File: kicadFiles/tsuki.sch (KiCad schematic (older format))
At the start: 203 parts, among them J1 TYPE-C-31-M12_13, J2 Conn_01x14, J3 Conn_ARM_JTAG_SWD_10, SW1 ESC, SW10 9, SW11 0, SW12 -_, SW13 +=, SW14 2U BKSP, SW15 TAB_150, SW16 Q, SW17 W, SW18 E, SW19 R, SW2 1, SW20 T, SW21 Y, SW22 U, SW23 I, SW24 O, SW25 P, SW26 [{, SW27 ]}, SW28 \\|_150, SW29 CAPS_175, SW3 2, SW30 A, SW31 S, SW32 D, SW33 F, SW34 G, SW35 H, SW36 J, SW37 K, SW38 L, SW39 :;, SW4 3, SW40 \"', SW41 ENTER_225, SW42 LSHIFT_225, SW43 Z, SW44 X, SW45 C, SW46 V, SW47 B, SW48 N, SW49 M, SW5 4, SW50 <,, SW51 >., SW52 ?/, SW53 RSHIFT_275, SW54 LCTRL_150, SW55 LGUI_100, SW56 LALT_150, SW57 SPACE_600, SW58 RALT_150, SW59 RGUI_150, SW6 5, SW60 RCTRL_150, SW61 FN_100, SW62 RSHIFT_175, SW63 STEPPED_CAPS_125, SW64 1U LBKSP, SW65 1U RBKSP, SW66 ISO_100, SW67 ISO_ENTER, SW68 LCTRL_125, SW69 LGUI_125, SW7 6, SW70 LGUI_100, SW71 LALT_125, SW72 LALT_150, SW73 SPACE_225, SW74 SPACE_225, SW75 SPACE_625, SW76 SPACE_125, SW77 SPACE_700, SW78 SPACE_275, SW79 SPACE_275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

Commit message: Removed split space options
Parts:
- removed D63, D64: 1N4148, acheron_Components:D_SOD-123, symbol Device:D
- removed SW73, SW74: SPACE_225, acheron_MX_SolderMask:MX225R, symbol acheronSymbols:MXSwitch
- removed SW76: SPACE_125, acheron_MX_SolderMask:MX125, symbol acheronSymbols:MXSwitch
- removed SW78, SW79: SPACE_275, acheron_MX_SolderMask:MX275R, symbol acheronSymbols:MXSwitch
- removed SW82: RALT_150, acheron_MX_SolderMask:MX150, symbol acheronSymbols:MXSwitch
- removed SW85: RGUI_125, acheron_MX_SolderMask:MX125, symbol acheronSymbols:MXSwitch
- removed SW87: RCTRL_125, acheron_MX_SolderMask:MX125, symbol acheronSymbols:MXSwitch
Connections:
- net labels removed: L4
- wire segments 446 -> 424
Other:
- note removed: "225-125-275 Bottom"
- note removed: "225-275 Bottom"

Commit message: Remove layouts, update li, add label, maintenance
- The split backspace layouts were removed. This decision was made because I reckoned a very small amount of people would use them, and the PCB is already very compromised material-wise as it is.

- The Acheron Library was updated, following the updates in other projects

- A label was added signalling the pre-Revision Alpha

- The footprints for the holes were all changed for the no-backside version, to avoid any unintended short-circuits

- Indicative documentation and arrows were added for the bottom row layouts to facilitate building the PCB
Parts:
- added L4: TsukiLabel, tsukiGraphics:tsukiLabel_30x12mm, symbol Mechanical:MountingHole
- H10, H2, H3, H5, H7, H9: footprint acheron_MountingHoles:MoutingHole_Oval_7mm_5.0x2.5mm -> acheron_MountingHoles:MoutingHole_Oval_BackOnly_7mm_5.0x2.5mm
- L2: footprint oshLogo:osh-logo -> acheron_Graphics:osh-logo
- RGUI_125, SW1, SW10, SW11, SW12, SW13, SW14, SW15, SW16, SW17, SW18, SW19, SW2, SW20, SW21, SW22, SW23, SW24, SW25, SW26, SW27, SW28, SW29, SW3, SW30, SW31, SW32, SW33, SW34, SW35, SW36, SW37, SW38, SW39, SW4, SW40, SW41, SW42, SW43, SW44, SW45, SW46, SW47, SW48, SW49, SW5, SW50, SW51, SW52, SW53, SW54, SW55, SW56, SW57, SW58, SW59, SW6, SW60, SW61, SW62, SW63, SW64, SW65, SW66, SW67, SW68, SW69, SW7, SW70, SW71, SW72, SW75, SW77, SW8, SW80, SW81, SW83, SW84, SW86, SW88, SW89, SW9: symbol acheronSymbols:MXSwitch -> tsuki-rescue:MXSwitch-acheronSymbols
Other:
- note added: "6.25U Bottom (D for default ANSI)"
- note added: "6U Bottom (H for HHKB)"
- note added: "7U Bottom (T for Tsangan bottom)"
- note removed: "6.25U Bottom"
- note removed: "6U Bottom"
- note removed: "7U Bottom"

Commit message: Added Schottky diodes and TVS
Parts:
- removed CUSB1: 100n, Capacitor_SMD:C_0805_2012Metric_Pad1.15x1.40mm_HandSolder, symbol Device:C_Small
- CSI1, CSO1: value 100n -> 1u
- DF1: value RB060M-60TR -> SMF9.0CA; symbol Device:D_Schottky -> Device:D_TVS
- DS1: value 1N4148 -> RB060M-60TR; symbol Device:D -> Device:D_Schottky
- DSH1: value 1N4007 -> RB060M-60TR; symbol Device:D -> Device:D_Schottky
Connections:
- wire segments 424 -> 421
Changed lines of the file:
@@
 P 8475 20600
 F 0 "CSI1" V 8575 20600 39  0000 C CNN
-F 1 "100n" V 8375 20600 31  0000 C CNN
+F 1 "1u" V 8375 20600 31  0000 C CNN
 F 2 "Capacitor_SMD:C_0805_2012Metric_Pad1.15x1.40mm_HandSolder" H 8475 20600 50  0001 C CNN
 F 3 "~" H 8475 20600 50  0001 C CNN
@@
 	-1   0    0    1
 $EndComp
-$Comp
-L Device:C_Small CSO1
-U 1 1 5C44DAFA
-P 9175 20625
-F 0 "CSO1" V 9275 20625 39  0000 C CNN
-F 1 "100n" V 9050 20625 39  0000 C CNN
-F 2 "Capacitor_SMD:C_0805_2012Metric_Pad1.15x1.40mm_HandSolder" H 9175 20625 50  0001 C CNN
-F 3 "~" H 9175 20625 50  0001 C CNN
-	1    9175 20625
-	-1   0    0    1
-$EndComp
 Wire Wire Line
 	9175 20250 9175 20525
@@
 	7275 19350 10250 19350
 $Comp
-L Device:D DS1
+L Device:D_Schottky DS1
 U 1 1 5C44EA7A
 P 8825 19775
 F 0 "DS1" V 8794 19854 31  0000 L CNN
-F 1 "1N4148" V 8856 19854 31  0000 L CNN
+F 1 "RB060M-60TR" V 8856 19854 31  0000 L CNN
 F 2 "acheron_Components:D_SOD-123" H 8825 19775 50  0001 C CNN
 F 3 "~" H 8825 19775 50  0001 C CNN
@@
 Wire Wire Line
 	5725 15175 5775 15175
-$Comp
-L Device:C_Small CUSB1
-U 1 1 5E01896F
-P 5375 14725
-F 0 "CUSB1" V 5275 14725 31  0000 C CNN
-F 1 "100n" V 5475 14725 31  0000 C CNN
-F 2 "Capacitor_SMD:C_0805_2012Metric_Pad1.15x1.40mm_HandSolder" H 5375 14725 50  0001 C CNN
-F 3 "~" H 5375 14725 50  0001 C CNN
-	1    5375 14725
-	0    1    1    0
-$EndComp
-Wire Wire Line
-	5225 14775 5225 14725
-Wire Wire Line
-	5275 14725 5225 14725
-Connection ~ 5225 14725
-Wire Wire Line
-	5475 14725 5525 14725
-$Comp
-L power:GND #PWR0112
-U 1 1 5E173141
-P 5525 14725
-F 0 "#PWR0112" H 5525 14475 50  0001 C CNN
-F 1 "GND" H 5525 14600 31  0000 C CNN
-F 2 "" H 5525 14725 50  0001 C CNN
-F 3 "" H 5525 14725 50  0001 C CNN
-	1    5525 14725
-	0    -1   -1   0
-$EndComp
 Text GLabel 5225 14650 1    50   Input ~ 0
 VBUS
-Wire Wire Line
-	5225 14650 5225 14725
 $Comp
 L power:GND #PWR0113
@@
 $EndComp
 $Comp
-L Device:D_Schottky DF1
+L Device:D_TVS DF1
 U 1 1 5ECEA097
 P 8100 20425
 F 0 "DF1" H 8050 20250 50  0000 L CNN
-F 1 "RB060M-60TR" H 7975 20325 30  0000 L CNN
+F 1 "SMF9.0CA" H 7975 20325 30  0000 L CNN
 F 2 "acheron_Components:D_SOD-123" H 8100 20425 50  0001 C CNN
 F 3 "~" H 8100 20425 50  0001 C CNN
@@
 $EndComp
 $Comp
-L Device:D DSH1
+L Device:D_Schottky DSH1
 U 1 1 5D48318C
 P 11575 17250
 F 0 "DSH1" V 11544 17329 31  0000 L CNN
-F 1 "1N4007" V 11606 17329 31  0000 L CNN
+F 1 "RB060M-60TR" V 11606 17329 31  0000 L CNN
 F 2 "acheron_Components:D_SOD-123" H 11575 17250 50  0001 C CNN
 F 3 "~" H 11575 17250 50  0001 C CNN
@@
 	1    0    0    -1
 $EndComp
+$Comp
+L Device:C_Small CSO1
+U 1 1 5C44DAFA
+P 9175 20625
+F 0 "CSO1" V 9275 20625 39  0000 C CNN
+F 1 "1u" V 9050 20625 39  0000 C CNN
+F 2 "Capacitor_SMD:C_0805_2012Metric_Pad1.15x1.40mm_HandSolder" H 9175 20625 50  0001 C CNN
+F 3 "~" H 9175 20625 50  0001 C CNN
+	1    9175 20625
+	-1   0    0    1
+$EndComp
+Wire Wire Line
+	5225 14650 5225 14775
 $EndSCHEMATC

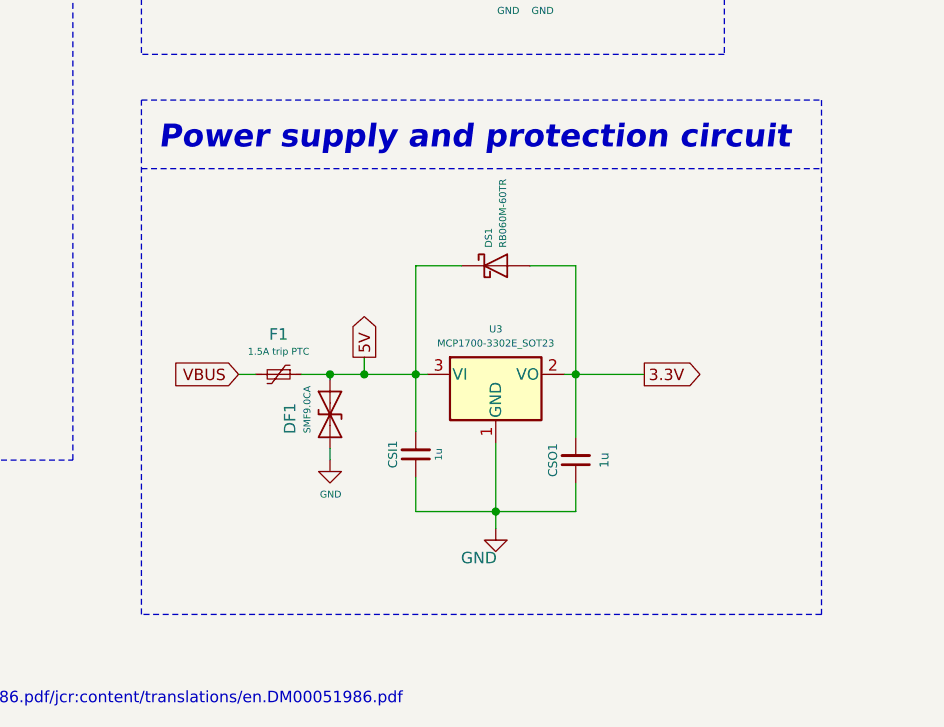
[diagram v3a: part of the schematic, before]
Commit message: Added discharge resistors RSI and RSO
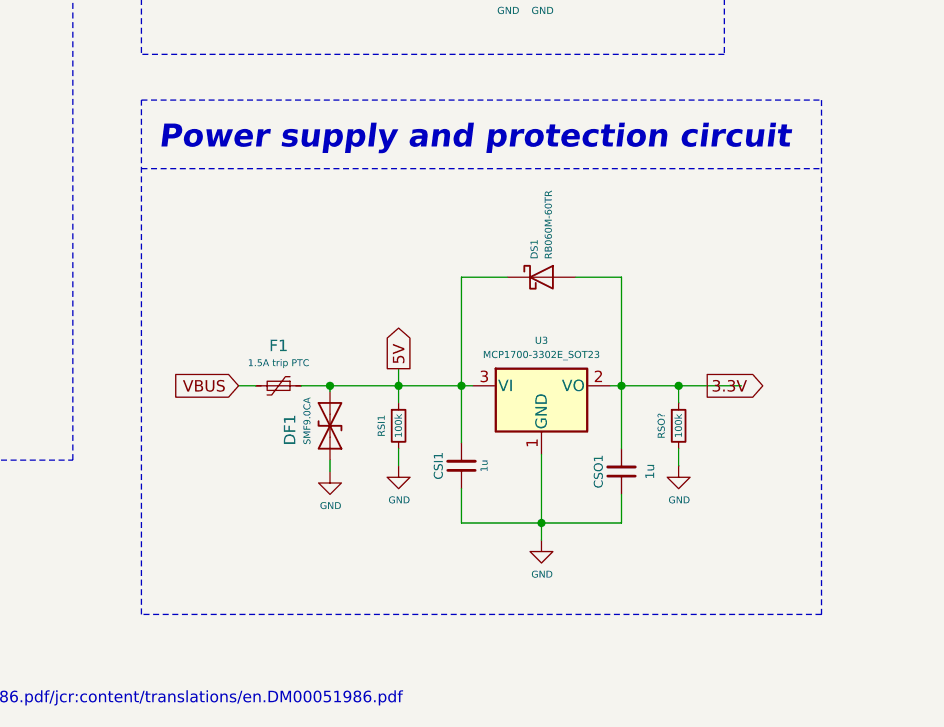
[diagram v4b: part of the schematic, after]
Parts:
- added RSI1, RSO?: 100k, acheron_Components:R_SMD_1206, symbol Device:R_Small
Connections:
- wire segments 421 -> 426
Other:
- moved on the sheet: CSI1, CSO1, DF1, DS1, F1, U3
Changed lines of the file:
@@
 L Device:C_Small CSI1
 U 1 1 5C44CEDC
-P 8475 20600
-F 0 "CSI1" V 8575 20600 39  0000 C CNN
-F 1 "1u" V 8375 20600 31  0000 C CNN
-F 2 "Capacitor_SMD:C_0805_2012Metric_Pad1.15x1.40mm_HandSolder" H 8475 20600 50  0001 C CNN
-F 3 "~" H 8475 20600 50  0001 C CNN
-	1    8475 20600
+P 8675 20650
+F 0 "CSI1" V 8775 20650 39  0000 C CNN
+F 1 "1u" V 8575 20650 31  0000 C CNN
+F 2 "Capacitor_SMD:C_0805_2012Metric_Pad1.15x1.40mm_HandSolder" H 8675 20650 50  0001 C CNN
+F 3 "~" H 8675 20650 50  0001 C CNN
+	1    8675 20650
 	-1   0    0    1
 $EndComp
 Wire Wire Line
-	9175 20250 9175 20525
+	9375 20300 9375 20575
 Wire Wire Line
-	8525 20250 8475 20250
+	8725 20300 8675 20300
 Wire Wire Line
-	8475 20250 8475 20500
-Connection ~ 8475 20250
+	8675 20300 8675 20550
+Connection ~ 8675 20300
 Wire Wire Line
-	8475 20250 8475 19775
-Wire Wire Line
-	8250 20250 8475 20250
-Text GLabel 9475 20250 2    50   Output ~ 0
+	8675 20300 8675 19825
+Text GLabel 9750 20300 2    50   Output ~ 0
 3.3V
 Text GLabel 20275 16700 2    50   BiDi ~ 0
@@
 L Regulator_Linear:MCP1700-3302E_SOT23 U3
 U 1 1 5D83639E
-P 8825 20250
-F 0 "U3" H 8825 20448 31  0000 C CNN
-F 1 "MCP1700-3302E_SOT23" H 8825 20386 31  0000 C CNN
-F 2 "Package_TO_SOT_SMD:SOT-23" H 8825 20475 50  0001 C CNN
-F 3 "http://ww1.microchip.com/downloads/en/DeviceDoc/20001826C.pdf" H 8825 20250 50  0001 C CNN
-	1    8825 20250
+P 9025 20300
+F 0 "U3" H 9025 20498 31  0000 C CNN
+F 1 "MCP1700-3302E_SOT23" H 9025 20436 31  0000 C CNN
+F 2 "Package_TO_SOT_SMD:SOT-23" H 9025 20525 50  0001 C CNN
+F 3 "http://ww1.microchip.com/downloads/en/DeviceDoc/20001826C.pdf" H 9025 20300 50  0001 C CNN
+	1    9025 20300
 	1    0    0    -1
 $EndComp
 Wire Wire Line
-	8475 20700 8475 20850
+	8675 20750 8675 20900
 Wire Wire Line
-	9175 20850 9175 20725
+	9375 20900 9375 20775
 Wire Wire Line
-	8825 20550 8825 20850
-Connection ~ 8825 20850
+	9025 20600 9025 20900
+Connection ~ 9025 20900
 Wire Wire Line
-	9125 20250 9175 20250
-$Comp
-L power:GND #PWR018
-U 1 1 5D9C16B4
-P 8825 20925
-F 0 "#PWR018" H 8825 20675 50  0001 C CNN
-F 1 "GND" H 8830 20797 50  0000 R CNN
-F 2 "" H 8825 20925 50  0001 C CNN
-F 3 "" H 8825 20925 50  0001 C CNN
-	1    8825 20925
-	1    0    0    -1
-$EndComp
+	9325 20300 9375 20300
 Wire Wire Line
-	8825 20925 8825 20850
+	9025 20975 9025 20900
 $Comp
 L Switch:SW_Push SWRST1
@@
 Text Notes 7350 19275 0    100  Italic 20
 Power supply and protection circuit
-Text GLabel 8250 20175 1    50   Output ~ 0
+Text GLabel 8400 20225 1    50   Output ~ 0
 5V
 Wire Wire Line
-	8250 20175 8250 20250
+	8400 20225 8400 20300
 Wire Wire Line
-	8975 19775 9175 19775
+	9175 19825 9375 19825
 Wire Wire Line
-	8475 19775 8675 19775
+	8675 19825 8875 19825
 Wire Wire Line
-	9175 20250 9175 19775
-Connection ~ 9175 20250
+	9375 20300 9375 19825
+Connection ~ 9375 20300
 Wire Wire Line
-	8825 20850 9175 20850
+	9025 20900 9375 20900
 Wire Wire Line
-	9175 20250 9475 20250
-Wire Wire Line
-	8825 20850 8475 20850
+	9025 20900 8675 20900
 Text GLabel 7900 18150 0    50   Input ~ 0
 3.3V
@@
 L Device:D_Schottky DS1
 U 1 1 5C44EA7A
-P 8825 19775
-F 0 "DS1" V 8794 19854 31  0000 L CNN
-F 1 "RB060M-60TR" V 8856 19854 31  0000 L CNN
-F 2 "acheron_Components:D_SOD-123" H 8825 19775 50  0001 C CNN
-F 3 "~" H 8825 19775 50  0001 C CNN
-	1    8825 19775
+P 9025 19825
+F 0 "DS1" V 8994 19904 31  0000 L CNN
+F 1 "RB060M-60TR" V 9056 19904 31  0000 L CNN
+F 2 "acheron_Components:D_SOD-123" H 9025 19825 50  0001 C CNN
+F 3 "~" H 9025 19825 50  0001 C CNN
+	1    9025 19825
 	1    0    0    -1
 $EndComp
@@
 L Device:Polyfuse_Small F1
 U 1 1 5ECE83A7
-P 7875 20250
-F 0 "F1" V 7700 20250 50  0000 C CNN
-F 1 "1.5A trip PTC" V 7775 20250 30  0000 C CNN
-F 2 "acheron_Components:Fuse_1812_4532" H 7925 20050 50  0001 L CNN
-F 3 "~" H 7875 20250 50  0001 C CNN
-	1    7875 20250
+P 7875 20300
+F 0 "F1" V 7700 20300 50  0000 C CNN
+F 1 "1.5A trip PTC" V 7775 20300 30  0000 C CNN
+F 2 "acheron_Components:Fuse_1812_4532" H 7925 20100 50  0001 L CNN
+F 3 "~" H 7875 20300 50  0001 C CNN
+	1    7875 20300
 	0    1    1    0
 $EndComp
@@
 L Device:D_TVS DF1
 U 1 1 5ECEA097
-P 8100 20425
-F 0 "DF1" H 8050 20250 50  0000 L CNN
-F 1 "SMF9.0CA" H 7975 20325 30  0000 L CNN
-F 2 "acheron_Components:D_SOD-123" H 8100 20425 50  0001 C CNN
-F 3 "~" H 8100 20425 50  0001 C CNN
-	1    8100 20425
+P 8100 20475
+F 0 "DF1" H 8050 20300 50  0000 L CNN
+F 1 "SMF9.0CA" H 7975 20375 30  0000 L CNN
+F 2 "acheron_Components:D_SOD-123" H 8100 20475 50  0001 C CNN
+F 3 "~" H 8100 20475 50  0001 C CNN
+	1    8100 20475
 	0    1    1    0
 $EndComp
 Wire Wire Line
-	7975 20250 8100 20250
-Connection ~ 8250 20250
-Wire Wire Line
-	8100 20250 8100 20275
+	7975 20300 8100 20300
 Wire Wire Line
-	8100 20575 8100 20625
-Connection ~ 8100 20250
+	8100 20300 8100 20325
 Wire Wire Line
-	8100 20250 8250 20250
+	8100 20625 8100 20675
+Connection ~ 8100 20300
 Wire Wire Line
-	7700 20250 7775 20250
-Text GLabel 7700 20250 0    50   Input ~ 0
+	7700 20300 7775 20300
+Text GLabel 7700 20300 0    50   Input ~ 0
 VBUS
 $Comp
 L power:GND #PWR0110
 U 1 1 5ED7F608
-P 8100 20625
-F 0 "#PWR0110" H 8100 20375 50  0001 C CNN
-F 1 "GND" H 8150 20475 30  0000 R CNN
-F 2 "" H 8100 20625 50  0001 C CNN
-F 3 "" H 8100 20625 50  0001 C CNN
-	1    8100 20625
+P 8100 20675
+F 0 "#PWR0110" H 8100 20425 50  0001 C CNN
+F 1 "GND" H 8150 20525 30  0000 R CNN
+F 2 "" H 8100 20675 50  0001 C CNN
+F 3 "" H 8100 20675 50  0001 C CNN
+	1    8100 20675
 	1    0    0    -1
 $EndComp
@@
 L Device:C_Small CSO1
 U 1 1 5C44DAFA
-P 9175 20625
-F 0 "CSO1" V 9275 20625 39  0000 C CNN
-F 1 "1u" V 9050 20625 39  0000 C CNN
-F 2 "Capacitor_SMD:C_0805_2012Metric_Pad1.15x1.40mm_HandSolder" H 9175 20625 50  0001 C CNN
-F 3 "~" H 9175 20625 50  0001 C CNN
-	1    9175 20625
+P 9375 20675
+F 0 "CSO1" V 9475 20675 39  0000 C CNN
+F 1 "1u" V 9250 20675 39  0000 C CNN
+F 2 "Capacitor_SMD:C_0805_2012Metric_Pad1.15x1.40mm_HandSolder" H 9375 20675 50  0001 C CNN
+F 3 "~" H 9375 20675 50  0001 C CNN
+	1    9375 20675
 	-1   0    0    1
 $EndComp
 Wire Wire Line
 	5225 14650 5225 14775
+$Comp
+L Device:R_Small RSI1
+U 1 1 5DFE1813
+P 8400 20475
+F 0 "RSI1" V 8325 20475 31  0000 C CNN
+F 1 "100k" V 8400 20475 31  0000 C CNN
+F 2 "acheron_Components:R_SMD_1206" H 8400 20475 50  0001 C CNN
+F 3 "~" H 8400 20475 50  0001 C CNN
+	1    8400 20475
+	1    0    0    -1
+$EndComp
+$Comp
+L power:GND #PWR?
+U 1 1 5E04A109
+P 8400 20650
+F 0 "#PWR?" H 8400 20400 50  0001 C CNN
+F 1 "GND" H 8450 20500 30  0000 R CNN
+F 2 "" H 8400 20650 50  0001 C CNN
+F 3 "" H 8400 20650 50  0001 C CNN
+	1    8400 20650
+	1    0    0    -1
+$EndComp
+Wire Wire Line
+	8400 20650 8400 20575
+Wire Wire Line
+	8400 20375 8400 20300
+Connection ~ 8400 20300
+Wire Wire Line
+	8400 20300 8675 20300
+$Comp
+L Device:R_Small RSO?
+U 1 1 5E0E3A96
+P 9625 20475
+F 0 "RSO?" V 9550 20475 31  0000 C CNN
+F 1 "100k" V 9625 20475 31  0000 C CNN
+F 2 "acheron_Components:R_SMD_1206" H 9625 20475 50  0001 C CNN
+F 3 "~" H 9625 20475 50  0001 C CNN
+	1    9625 20475
+	1    0    0    -1
+$EndComp
+$Comp
+L power:GND #PWR?
+U 1 1 5E0E3A9D
+P 9625 20650
+F 0 "#PWR?" H 9625 20400 50  0001 C CNN
+F 1 "GND" H 9675 20500 30  0000 R CNN
+F 2 "" H 9625 20650 50  0001 C CNN
+F 3 "" H 9625 20650 50  0001 C CNN
+	1    9625 20650
+	1    0    0    -1
+$EndComp
+Wire Wire Line
+	9625 20650 9625 20575
+Wire Wire Line
+	9625 20375 9625 20300
+Connection ~ 9625 20300
+Wire Wire Line
+	9625 20300 9900 20300
+Wire Wire Line
+	9375 20300 9625 20300
+$Comp
+L power:GND #PWR?
+U 1 1 5E1B9CA9
+P 9025 20975
+F 0 "#PWR?" H 9025 20725 50  0001 C CNN
+F 1 "GND" H 9075 20825 30  0000 R CNN
+F 2 "" H 9025 20975 50  0001 C CNN
+F 3 "" H 9025 20975 50  0001 C CNN
+	1    9025 20975
+	1    0    0    -1
+$EndComp
+Wire Wire Line
+	8100 20300 8400 20300
 $EndSCHEMATC

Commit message: Added RGB to schematic
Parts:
- added CRGB1, CRGB10, CRGB2, CRGB3, CRGB4, CRGB5, CRGB6, CRGB7, CRGB8, CRGB9: 100n, Capacitor_SMD:C_0805_2012Metric, symbol Device:C_Small
- added Q1: BSS138, Package_TO_SOT_SMD:SOT-23, symbol Transistor_FET:BSS138
- added RGB1, RGB10, RGB2, RGB3, RGB4, RGB5, RGB6, RGB7, RGB8, RGB9: WS2812B, LED_SMD:LED_WS2812B_PLCC4_5.0x5.0mm_P3.2mm, symbol LED:WS2812B
- added RRGB1, RRGB10, RRGB2, RRGB3, RRGB4, RRGB5, RRGB6, RRGB7, RRGB8, RRGB9: 5.1R, acheron_Components:R_SMD_1026, symbol Device:R_Small
- added RS1, RS2: 10k, acheron_Components:R_SMD_1026, symbol Device:R_Small
- gave numbers to parts that had none: 1
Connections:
- net labels added: RGB_3V3, RGB_5V
- wire segments 426 -> 507

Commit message: Added LED control to schematic
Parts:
- removed SW57: SPACE_600, acheron_MX_SolderMask:MX600R, symbol tsuki-rescue:MXSwitch-acheronSymbols
- added LED1: LED, acheron_Components:LED_THT_2.54mm, symbol acheronSymbols:LED
- added Q?: AO4407A, acheron_Components:SOIC-8, symbol tsuki-rescue:AO4407A-acheronSymbols
- added QRST?: DTC123J, Package_TO_SOT_SMD:SOT-23, symbol Transistor_BJT:DTC123J
- added RL1: 420R, acheron_Components:R_SMD_1206, symbol Device:R_Small
- added RLED1, RLED?: 10k, acheron_Components:R_SMD_1206, symbol Device:R_Small
- added RLED?: 100R, acheron_Components:R_SMD_1206, symbol Device:R_Small
- J1: symbol acheronSymbols:TYPE-C-31-M12_13 -> tsuki-rescue:TYPE-C-31-M12_13-acheronSymbols
- RCC1, RCC2, RRGB1, RRGB10, RRGB2, RRGB3, RRGB4, RRGB5, RRGB6, RRGB7, RRGB8, RRGB9, RRST1, RS1, RS2, RSH1, RSH2: footprint acheron_Components:R_SMD_1026 -> acheron_Components:R_SMD_1206
- RGB1, RGB10, RGB2, RGB3, RGB4, RGB5, RGB6, RGB7, RGB8, RGB9: footprint LED_SMD:LED_WS2812B_PLCC4_5.0x5.0mm_P3.2mm -> acheron_Components:LED_WS2812B_5.0x5.0mm_P3.2mm
- U1: symbol acheronSymbols:STM32F072-LQFP48 -> tsuki-rescue:STM32F072-LQFP48-acheronSymbols
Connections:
- net labels added: LED_PWM
- wire segments 507 -> 520
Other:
- note added: "Observation: the 6U spacebar footprint\nis already covered by the 6.25+7U\nspacebar footprints"

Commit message: Added bottom row documentation
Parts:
- added L5, L6, L7, L8, L9: Warning, acheron_Graphics:warning_sign_3.6x3.2mm, symbol Mechanical:MountingHole
- added LED10, LED11, LED12, LED13, LED14, LED15, LED16, LED17, LED18, LED19, LED2, LED20, LED21, LED22, LED23, LED24, LED25, LED26, LED27, LED28, LED29, LED3, LED30, LED31, LED32, LED4, LED5, LED6, LED7, LED8, LED9: LED, acheron_Components:LED_THT_2.54mm, symbol tsuki-rescue:LED-acheronSymbols
- added RL10, RL11, RL12, RL13, RL14, RL16, RL17, RL18, RL19, RL2, RL20, RL21, RL22, RL23, RL24, RL25, RL26, RL27, RL28, RL29, RL3, RL30, RL31, RL32, RL4, RL5, RL6, RL7, RL8, RL9: 420R, acheron_Components:R_SMD_1206, symbol Device:R_Small
- LED1: symbol acheronSymbols:LED -> tsuki-rescue:LED-acheronSymbols
- SW67: footprint acheron_MX_SolderMask:MX_ISOEnter_Vertical -> acheron_MX_SolderMask:MX_ISOEnter_Vertical_LED
- gave numbers to parts that had none: 4
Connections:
- net Col1: now also SW63.2 (Row); no longer SW63.1 (Col)
- net Col2: now also SW55.2 (Row); no longer SW55.1 (Col)
- net GND: now also LED10.K, LED11.K, LED12.K, LED13.K, LED14.K, LED15.K, LED16.K, LED17.K, LED18.K, LED19.K, LED2.K, LED20.K, LED21.K, LED22.K, LED23.K, LED24.K, LED25.K, LED26.K, LED27.K, LED28.K, LED29.K, LED3.K, LED30.K, LED31.K, LED32.K, LED4.K, LED5.K, LED6.K, LED7.K, LED8.K, LED9.K
- net L2: now also SW55.1 (Col); no longer SW55.2 (Row)
- net at D29.2 (A), SW29.2 (Row): now also SW63.1 (Col); no longer SW63.2 (Row)
- net at Q2.1 (S), Q2.2 (S), Q2.3 (S)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: now also RL10.2, RL11.2, RL12.2, RL13.2, RL14.2, RL16.2, RL17.2, RL18.2, RL19.2, RL2.2, RL20.2, RL21.2, RL22.2, RL23.2, RL24.2, RL25.2, RL26.2, RL27.2, RL28.2, RL29.2, RL3.2, RL30.2, RL31.2, RL32.2, RL4.2, RL5.2, RL6.2, RL7.2, RL8.2, RL9.2
- new net: LED2.A, RL2.1
- new net: LED3.A, RL3.1
- new net: LED4.A, RL4.1
- new net: LED5.A, RL5.1
- new net: LED6.A, RL6.1
- new net: LED7.A, RL7.1
- new net: LED8.A, RL8.1
- new net: LED9.A, RL9.1
- new net: LED10.A, RL10.1
- new net: LED11.A, RL11.1
- new net: LED12.A, RL12.1
- new net: LED13.A, RL13.1
- new net: LED14.A, LED15.A, RL14.1
- new net: LED16.A, RL16.1
- new net: LED17.A, RL17.1
- new net: LED18.A, RL18.1
- new net: LED19.A, RL19.1
- new net: LED20.A, RL20.1
- new net: LED21.A, RL21.1
- new net: LED22.A, RL22.1
- new net: LED23.A, RL23.1
- new net: LED24.A, RL24.1
- new net: LED25.A, RL25.1
- new net: LED26.A, RL26.1
- new net: LED27.A, RL27.1
- new net: LED28.A, RL28.1
- new net: LED29.A, RL29.1
- new net: LED30.A, RL30.1
- new net: LED31.A, RL31.1
- new net: LED32.A, RL32.1
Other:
- moved on the sheet: LED1

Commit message: Routed second row LEDs
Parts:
- removed D60: 1N4148, acheron_Components:D_SOD-123, symbol Device:D
- added LED33, LED34, LED35, LED36, LED37, LED38, LED39, LED40, LED41, LED42, LED43, LED44, LED45, LED46, LED47, LED48: LED, acheron_Components:LED_THT_2.54mm, symbol tsuki-rescue:LED-acheronSymbols
- added RGND1: R01, acheron_Components:R_SMD_1206, symbol Device:R_Small
- added RL15, RL33, RL34, RL35, RL36, RL37, RL38, RL39, RL40, RL41, RL42, RL43, RL44, RL45, RL46, RL47: 420R, acheron_Components:R_SMD_1206, symbol Device:R_Small
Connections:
- net labels added: GNDD
- wire segments 646 -> 709
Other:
- moved on the sheet: D28, D41, D58, D59, RGUI_125, SW28, SW41, SW58, SW59, SW60, SW67, SW81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
